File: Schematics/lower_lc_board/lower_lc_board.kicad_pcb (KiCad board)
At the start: 4 copper layers, 69.5 x 60 mm, 140 parts, among them J1 Stack Male Edge Connector, J10 SOL_CONN, J3 USB_C_CONN, J4 HALL-1, J5 HALL-2, J6 PT1, J7 Screw_Terminal_01x02, J8 PT1, J9 SOL_CONN, Q1 AO3400A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

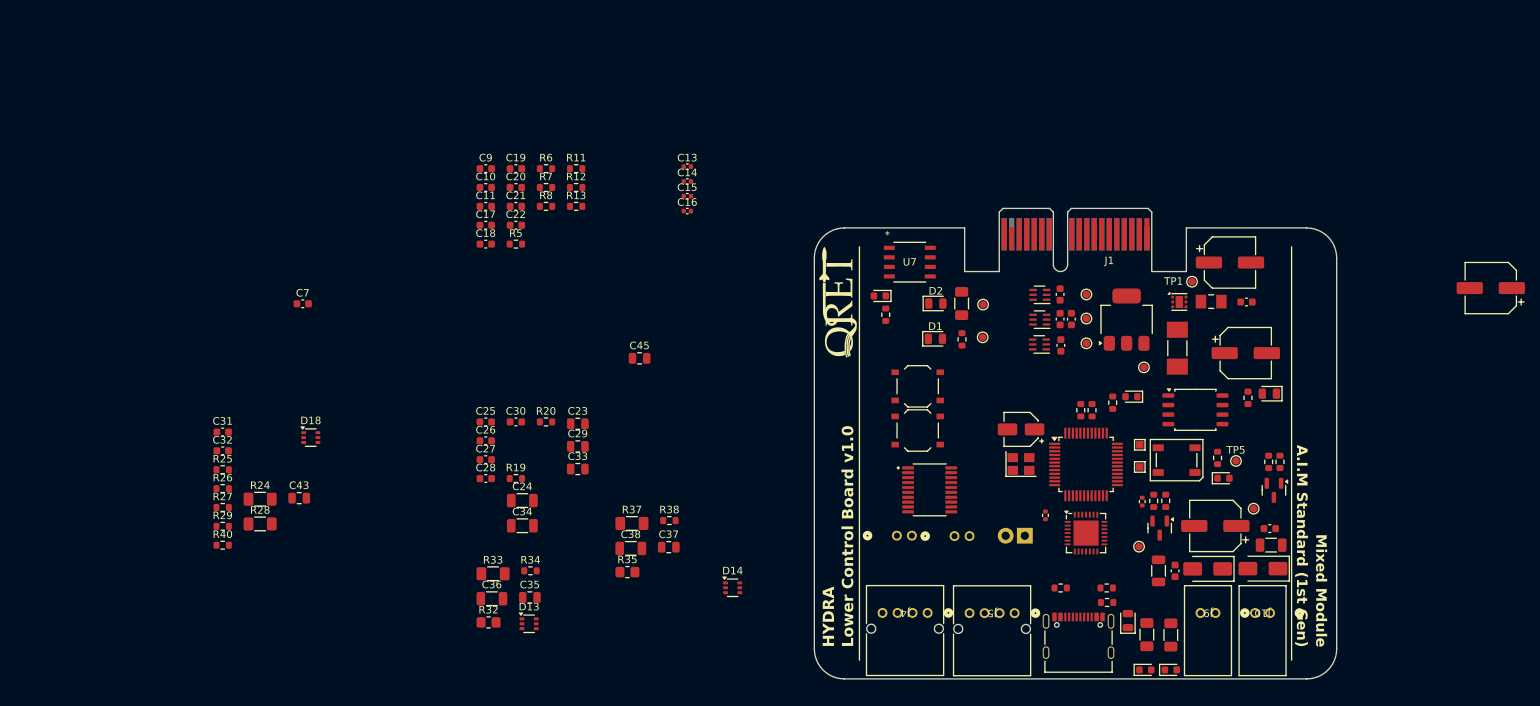
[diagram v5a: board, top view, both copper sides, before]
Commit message: add sensing circuitry layout
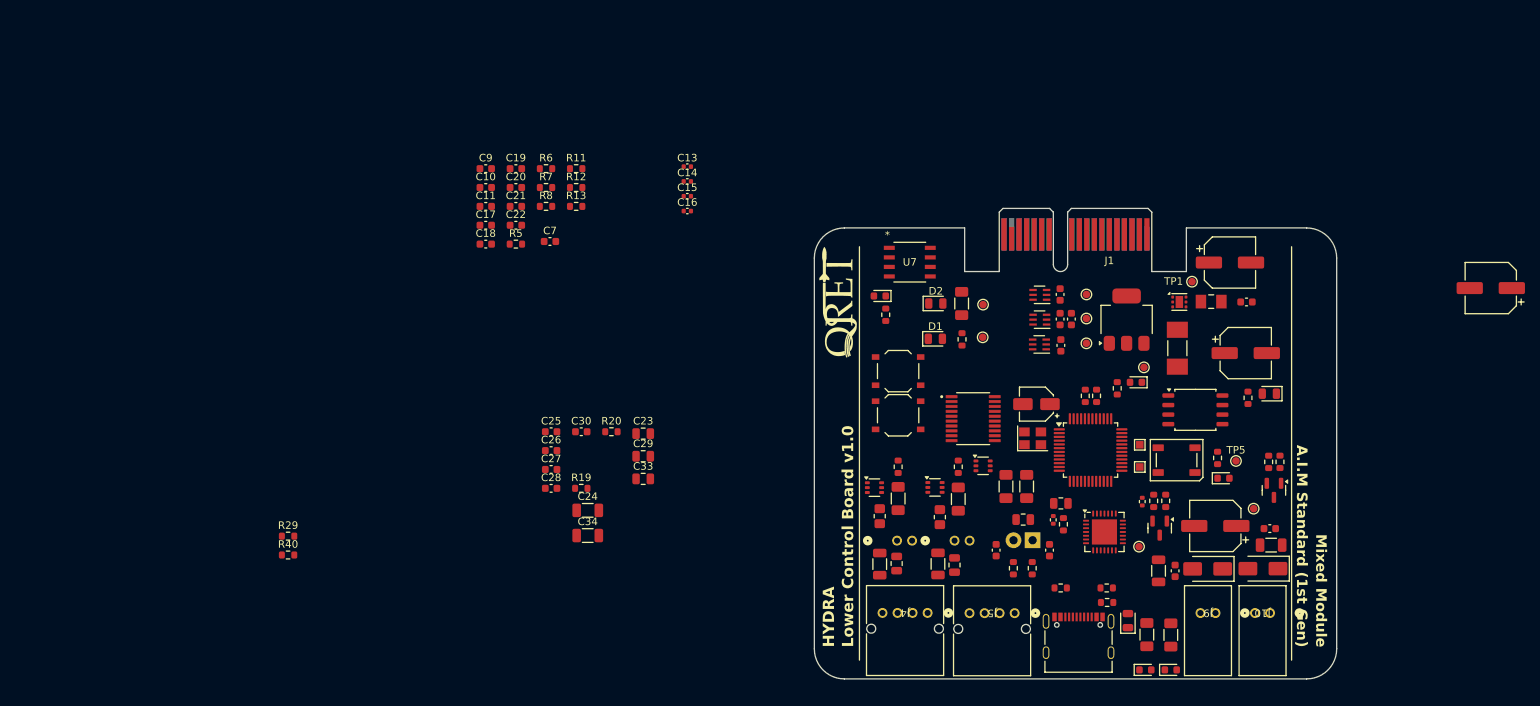
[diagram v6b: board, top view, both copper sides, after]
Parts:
- moved R25 112.1 mm to (153.7, 87.0), turned to -90 degrees
- moved C31 111.1 mm to (151.9, 90.4), turned to 90 degrees
- moved R26 108.2 mm to (149.6, 92.8), turned to 90 degrees
- moved R27 105.5 mm to (147.1, 92.8), turned to -90 degrees
- moved C32 103.8 mm to (144.8, 90.4), turned to 90 degrees
- moved R24 102.0 mm to (148.8, 82.0), turned to -90 degrees
- moved R28 99.4 mm to (146.1, 82.0), turned to -90 degrees
- moved C43 96.4 mm to (148.4, 86.3)
- moved D18 89.5 mm to (143.1, 79.2)
- moved C45 59.3 mm to (153.4, 84.2), turned to 180 degrees
- moved R33 54.8 mm to (131.8, 83.5), turned to 90 degrees
- moved R32 53.9 mm to (129.3, 85.9), turned to 90 degrees
- moved C36 51.8 mm to (129.3, 92.3), turned to -90 degrees
- moved R34 50.8 mm to (131.8, 79.3), turned to -90 degrees
- moved D13 49.4 mm to (128.6, 82.1)
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
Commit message: finish layout
- model paths need to be fixed
- waiting for confirmation for shared folders
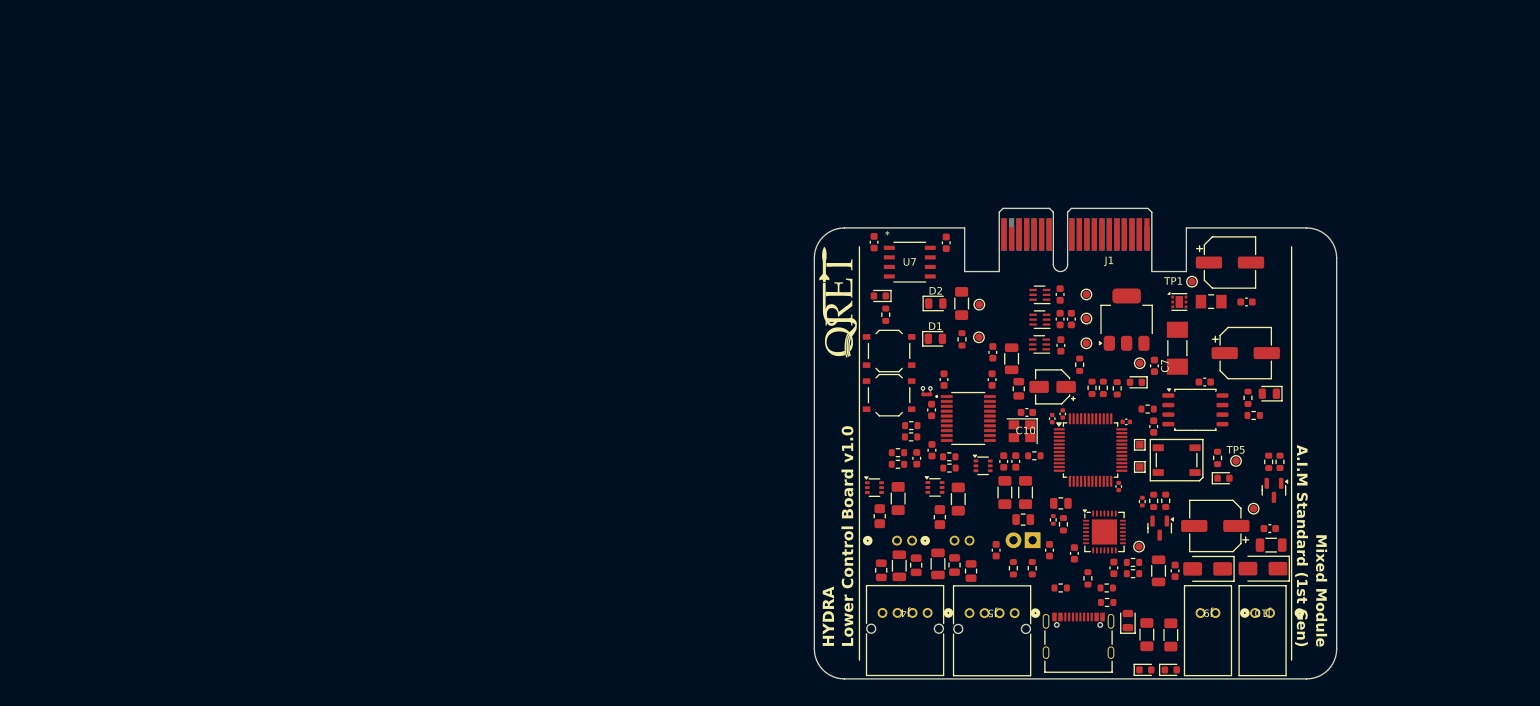
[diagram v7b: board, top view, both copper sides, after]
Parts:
- removed C24, C34: 1uF_10V, Capacitor_SMD:C_1206_3216Metric
- added C47: 0.1uF_16V, Capacitor_SMD:C_0603_1608Metric, F.Cu at (144.3, 64.1)
- added NT1: GND-TIE, NetTie:NetTie-2_SMD_Pad0.5mm, F.Cu at (135.6, 69.7)
- C1: value 100uF_16V -> 47uF_16V; footprint Capacitor_SMD:CP_Elec_6.3x5.9 -> Capacitor_SMD:C_1206_3216Metric
- moved R7 98.9 mm to (179.1, 72.5)
- moved C17 97.9 mm to (172.6, 68.0), turned to 180 degrees
- moved C20 94.3 mm to (160.4, 92.8), turned to 90 degrees
- moved R11 90.7 mm to (163.0, 92.0)
- moved R12 90.2 mm to (163.0, 93.5), turned to 180 degrees
- moved C22 89.0 mm to (165.8, 74.0), turned to 90 degrees
- moved C21 87.5 mm to (155.2, 90.8), turned to 90 degrees
- moved R8 84.5 mm to (164.9, 71.7), turned to 180 degrees
- moved R40 84.4 mm to (133.5, 75.3)
- moved R29 84.2 mm to (133.5, 73.8)
- moved R13 84.2 mm to (157.0, 94.2), turned to -90 degrees
- moved C7 82.1 mm to (165.8, 65.9), turned to -90 degrees
- moved C9 80.6 mm to (147.4, 78.6), turned to 90 degrees
- moved C10 78.0 mm to (148.9, 72.1), turned to 180 degrees
- moved C11 76.8 mm to (145.8, 78.6), turned to -90 degrees
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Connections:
- C28 pad 1: GND -> GNDA
- C29 pad 2: GND -> GNDA
- C31 pad 1: GND -> GNDA
- C32 pad 1: GND -> GNDA
- C35 pad 2: GND -> GNDA
- C36 pad 2: GND -> GNDA
- C37 pad 2: GND -> GNDA
- C38 pad 2: GND -> GNDA
- D13 pad 1: GND -> GNDA
- D14 pad 1: GND -> GNDA
- D18 pad 1: GND -> GNDA
- D18 pad 4: GND -> GNDA
- R19 pad 1: GND -> GNDA
- R20 pad 1: GND -> GNDA
- R27 pad 2: GND -> GNDA
- R32 pad 1: GND -> GNDA
- R35 pad 1: GND -> GNDA
- TH1 pad 2: GND -> GNDA
- U9 pad 2: GND -> GNDA
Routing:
- net GNDA: track 0.00 -> 0.80 mm, vias 0 -> 1
- net GND: track 0.00 -> 0.80 mm, vias 0 -> 1

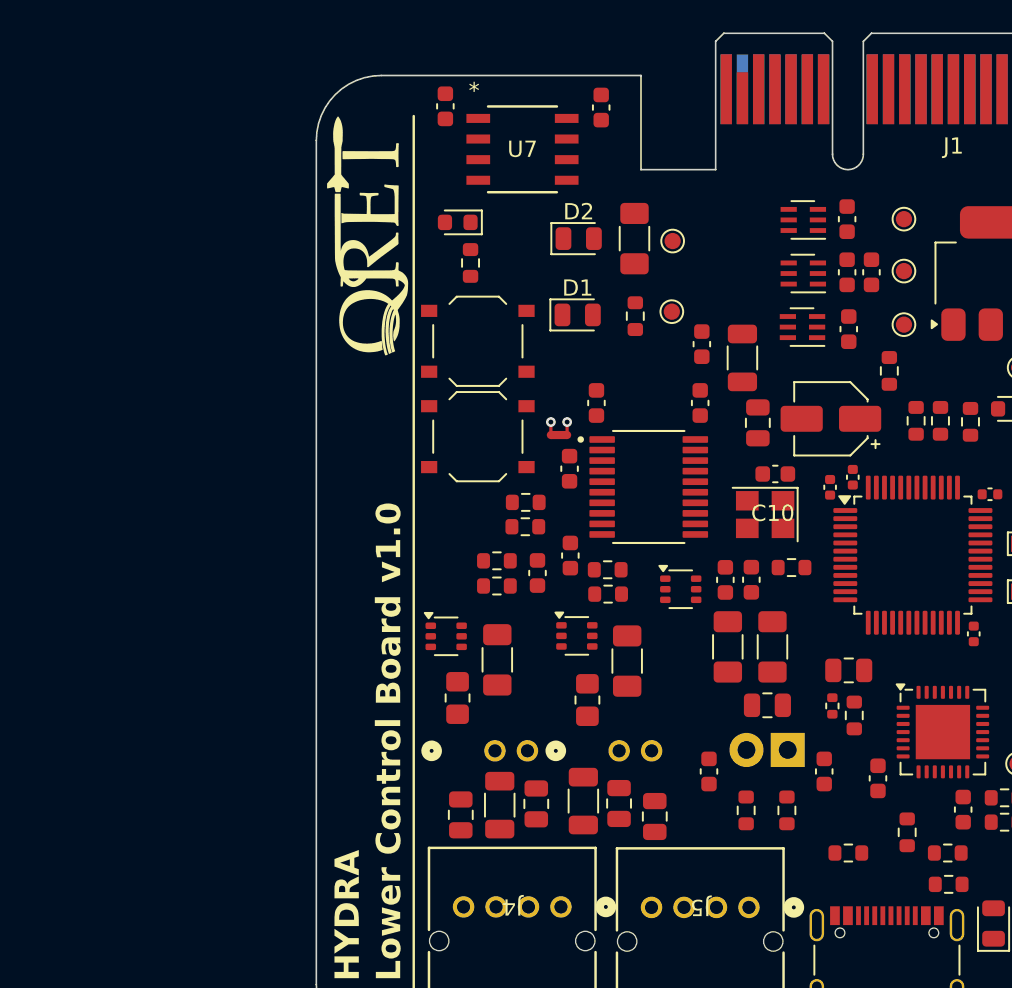
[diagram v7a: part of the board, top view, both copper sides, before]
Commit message: add power switching for PTs (schematic only)
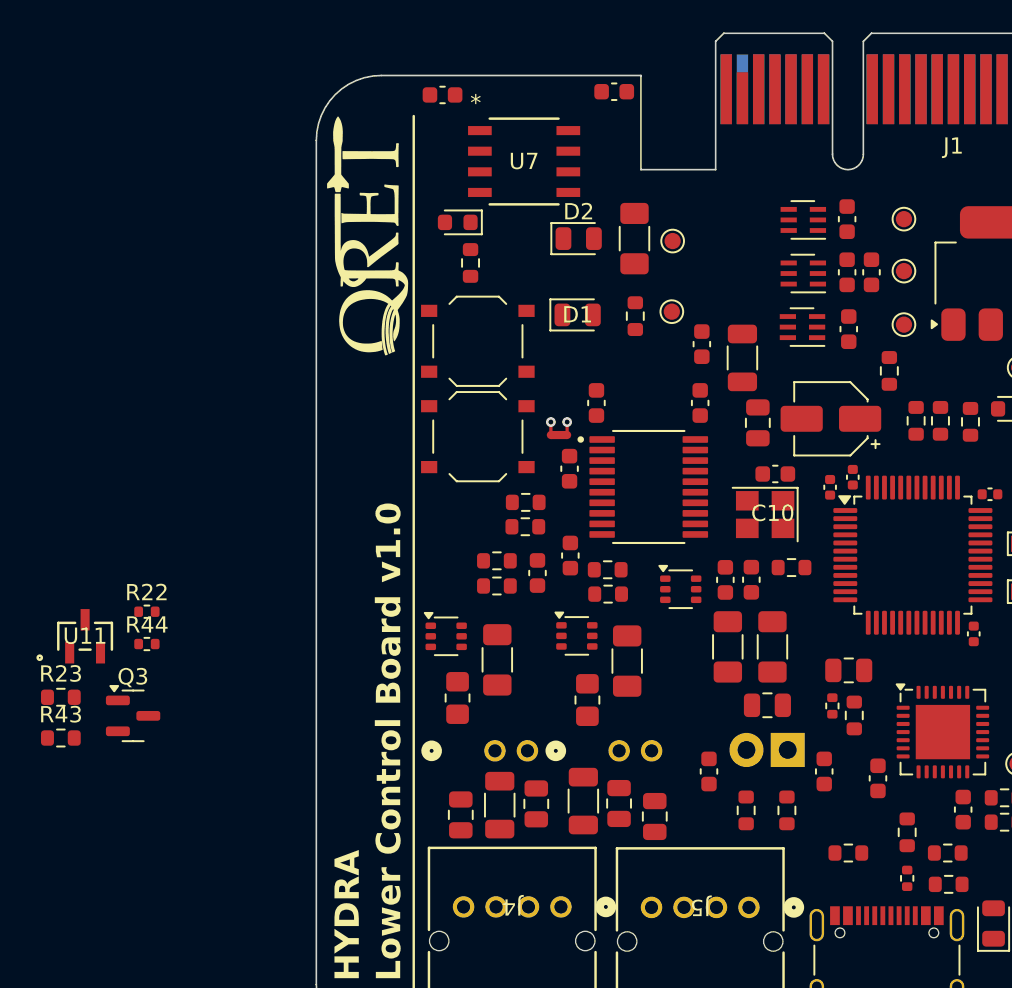
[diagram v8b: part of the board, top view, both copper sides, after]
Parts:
- added Q3: 2N7002, Package_TO_SOT_SMD:SOT-23, F.Cu at (109.3, 87.0)
- added R22: 10k, Resistor_SMD:R_0402_1005Metric, F.Cu at (110.2, 80.6)
- added R23: 10k, Resistor_SMD:R_0603_1608Metric, F.Cu at (104.9, 85.9)
- added R43: 10k, Resistor_SMD:R_0603_1608Metric, F.Cu at (104.9, 88.4)
- added R44: 200, Resistor_SMD:R_0402_1005Metric, F.Cu at (110.2, 82.6)
- added R45: 1.5k, Resistor_SMD:R_0402_1005Metric, F.Cu at (157.0, 97.0)
- added U11: SI2301CDS-T1-GE3, ul_SI2301CDS-T1-GE3:TO-236_VIS, F.Cu at (106.4, 82.1)
- moved C19 1.26 mm to (138.9, 48.5), turned to 0 degrees
- moved U7 0.76 mm to (133.4, 52.9)
- moved C18 0.72 mm to (128.4, 48.8), turned to 0 degrees
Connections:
- C35 pad 1: +24V -> /Sensing Circuitry/VPT
- C36 pad 1: +24V -> /Sensing Circuitry/VPT
- C37 pad 1: +24V -> /Sensing Circuitry/VPT
- C38 pad 1: +24V -> /Sensing Circuitry/VPT
- J6 pad 1: +24V -> /Sensing Circuitry/VPT
- J8 pad 1: +24V -> /Sensing Circuitry/VPT
